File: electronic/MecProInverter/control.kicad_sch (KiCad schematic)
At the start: 30 parts, among them J5 Conn_01x08, SW1 PTS645SM95SMTR92LFS, SW2 PTS645SM95SMTR92LFS, SW3 PTS645SM95SMTR92LFS, U1 ESP32-S3-MINI-1-N8, U2 ADUM3160, U3 TYPE-C_16PIN_2MD(073), U6 SKRKAEE020, U7 SKRKAEE020

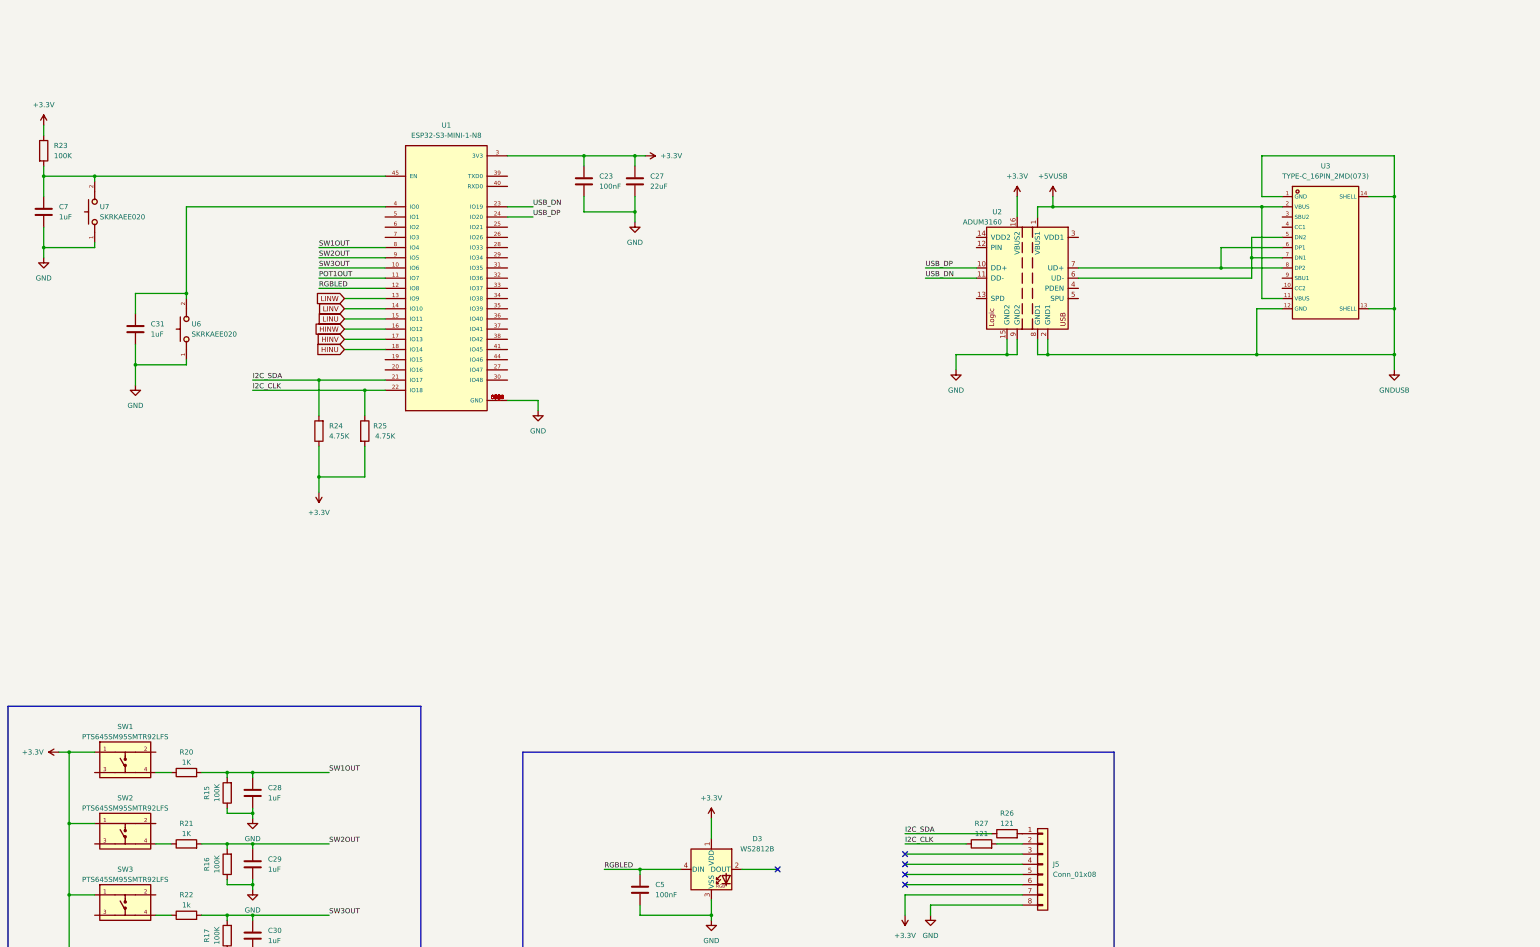
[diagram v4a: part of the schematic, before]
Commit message: electronic
-Control: Added Temp, Fan,
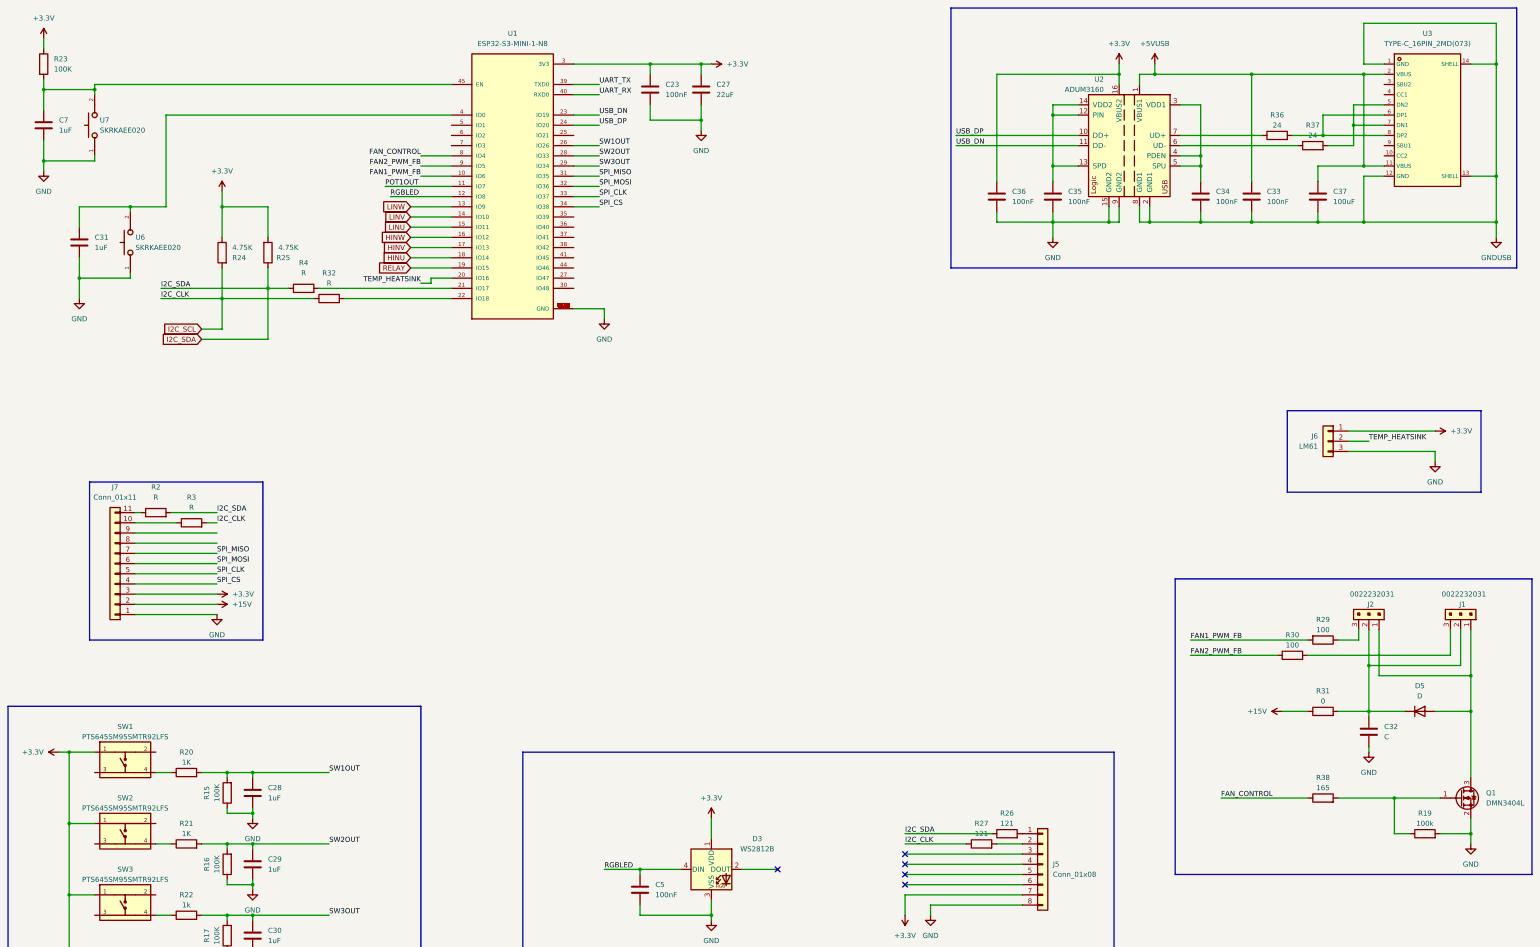
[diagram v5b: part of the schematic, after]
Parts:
- added C32: C, symbol Device:C
- added C33, C34, C35, C36: 100nF, symbol Device:C
- added C37: 100uF, symbol Device:C
- added D5: D, symbol Device:D
- added J1, J2: 0022232031, digikey-footprints:PinHeader_1x3_P2.54mm_Drill1.02mm, symbol dk_Rectangular-Connectors-Headers-Male-Pins:0022232031
- added J6: LM61, symbol Connector_Generic:Conn_01x03
- added J7: Conn_01x11, symbol Connector_Generic:Conn_01x11
- added Q1: DMN3404L, Package_TO_SOT_SMD:SOT-23, symbol Transistor_FET:DMN3404L
- added R19: 100k, symbol Device:R
- added R2, R3, R32, R4: R, symbol Device:R
- added R29, R30: 100, symbol Device:R
- added R31: 0, symbol Device:R
- added R36, R37: 24, symbol Device:R
- added R38: 165, symbol Device:R
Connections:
- net +3.3V: now also C36.1, J6.1 (Pin_1), J7.3 (Pin_3)
- net +5V: now also C33.1, C37.1
- net GND: now also C32.2, C33.2, C34.2, C35.2, C36.2, C37.2, J6.3 (Pin_3), J7.1 (Pin_1), Q1.2 (S), R19.2
- net I2C_SDA: now also R25.1, R2.2, R4.1; no longer R24.2, U1.21 (IO17)
- net SW1OUT: now also U1.26 (IO26); no longer U1.8 (IO4)
- net SW2OUT: now also U1.28 (IO33); no longer U1.9 (IO5)
- net SW3OUT: now also U1.29 (IO34); no longer U1.10 (IO6)
- net at U2.12 (PIN): now also U2.13 (SPD), U2.14 (VDD2), C35.1
- net at U2.3 (VDD1): now also U2.4 (PDEN), U2.5 (SPU), C34.1
- net at U3.5 (DN2), U3.7 (DN1): now also R37.2; no longer U2.6 (UD-)
- net at U3.6 (DP1), U3.8 (DP2): now also R36.2; no longer U2.7 (UD+)
- net RELAY: now reaches U1.19 (IO15)
- net TEMP_HEATSINK: now reaches U1.20 (IO16)
- net TEMP_HEATSINK: now also J6.2 (Pin_2)
- net SPI_MISO: now reaches U1.31 (IO35)
- net SPI_MISO: now also J7.7 (Pin_7)
- net SPI_MOSI: now reaches U1.32 (IO36)
- net SPI_MOSI: now also J7.6 (Pin_6)
- net SPI_CLK: now reaches U1.33 (IO37)
- net SPI_CLK: now also J7.5 (Pin_5)
- net SPI_CS: now reaches U1.34 (IO38)
- net SPI_CS: now also J7.4 (Pin_4)
- net UART_TX: now reaches U1.39 (TXD0)
- net UART_RX: now reaches U1.40 (RXD0)
- removed net I2C_CLK: R25.1, R27.1, U1.22 (IO18)
- new net: J7.10 (Pin_10), R3.1
- new net: J2.3, R29.1
- new net: Q1.1 (G), R19.1, R38.2
- new net: R37.1, U2.6 (UD-)
- new net: R36.1, U2.7 (UD+)
- new net: D5.2 (A), J1.1, J2.1, Q1.3 (D)
- new net: C32.1, D5.1 (K), J1.2, J2.2, R31.2
- new net: J1.3, R30.2
- new net: R4.2, U1.21 (IO17)
- new net: R32.2, U1.22 (IO18)
- new net: J7.11 (Pin_11), R2.1
- new net +15V: J7.2 (Pin_2), R31.1
- new net FAN1_PWM_FB: R29.2, U1.10 (IO6)
- new net FAN2_PWM_FB: R30.1, U1.9 (IO5)
- new net FAN_CONTROL: R38.1, U1.8 (IO4)
- new net I2C_SCL: R24.2, R27.1, R3.2, R32.1
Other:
- moved on the sheet: C23, C27, C31, C7, R23, R24, R25, U1, U2, U3, U6, U7

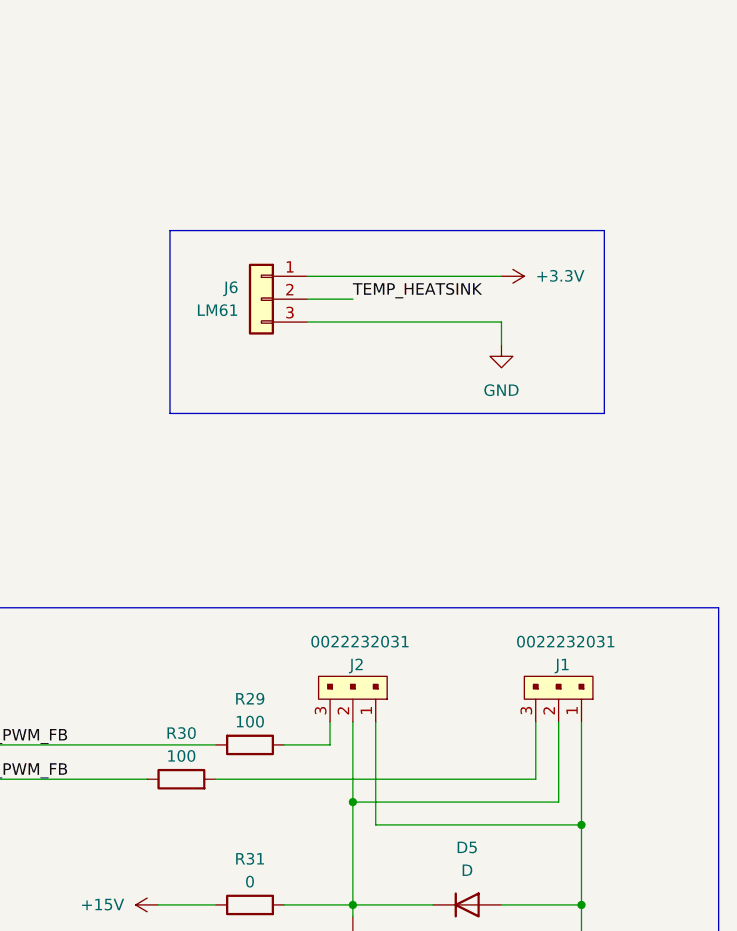
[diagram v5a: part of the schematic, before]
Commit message: electronic
Added: current sensor
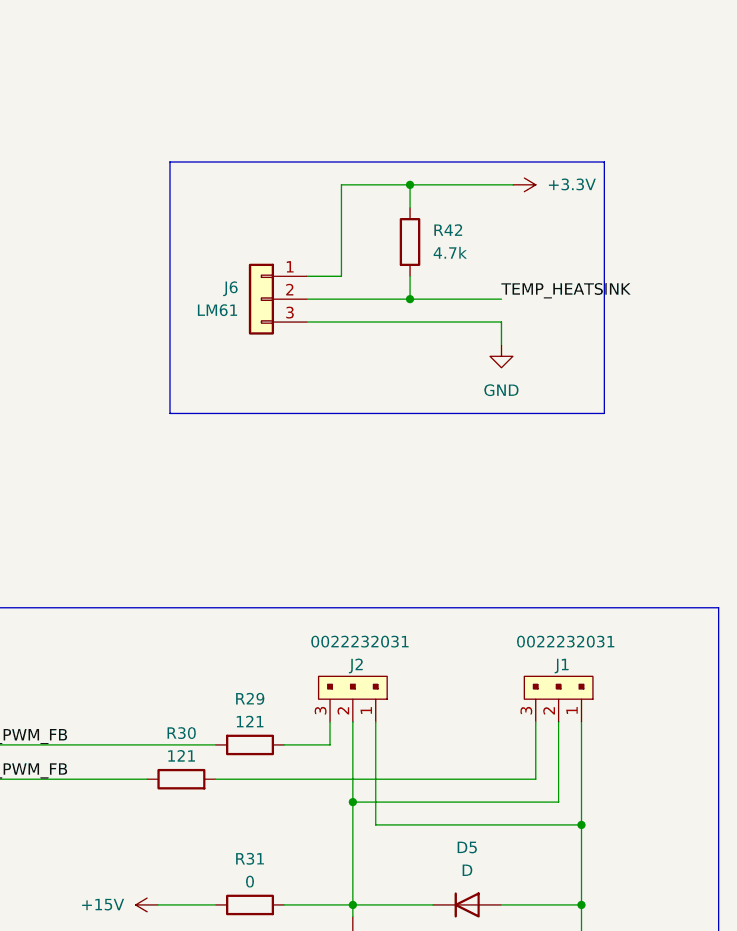
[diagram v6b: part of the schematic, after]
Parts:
- added R42: 4.7k, symbol Device:R
- J5: footprint (none) -> Connector_PinSocket_2.54mm:PinSocket_1x08_P2.54mm_Vertical
- J6: footprint (none) -> Connector_PinHeader_2.54mm:PinHeader_1x03_P2.54mm_Vertical
- J7: footprint (none) -> Connector_PinHeader_2.54mm:PinHeader_1x11_P2.54mm_Vertical
- R29, R30: value 100 -> 121
- U1: footprint ESP32-S3-MINI-1-N8:XCVR_ESP32-S3-MINI-1-N8 -> footprint:BULETM-SMD_ESP32-S3-MINI-1-N8
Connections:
- net +3.3V: now also R42.1
- net TEMP_HEATSINK: now also R42.2
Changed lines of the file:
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@@
   (junction (at 26.67 58.42) (diameter 0) (color 0 0 0 0)
   )
+  (junction (at 363.22 128.27) (diameter 0) (color 0 0 0 0)
+  )
   (junction (at 72.39 246.38) (diameter 0) (color 0 0 0 0)
   )
@@
   (junction (at 356.87 184.15) (diameter 0) (color 0 0 0 0)
   )
+  (junction (at 363.22 115.57) (diameter 0) (color 0 0 0 0)
+  )
   (junction (at 71.12 92.71) (diameter 0) (color 0 0 0 0)
   )
@@
     (stroke (width 0) (type default))
   )
-  (wire (pts (xy 373.38 125.73) (xy 351.79 125.73))
+  (wire (pts (xy 374.65 115.57) (xy 363.22 115.57))
     (stroke (width 0) (type default))
   )
@@
     (stroke (width 0) (type default))
   )
+  (wire (pts (xy 355.6 125.73) (xy 351.79 125.73))
+    (stroke (width 0) (type default))
+  )
+  (wire (pts (xy 363.22 125.73) (xy 363.22 128.27))
+    (stroke (width 0) (type default))
+  )
   (wire (pts (xy 66.04 210.82) (xy 72.39 210.82))
     (stroke (width 0) (type default))
@@
     (stroke (width 0) (type default))
   )
+  (wire (pts (xy 363.22 115.57) (xy 363.22 118.11))
+    (stroke (width 0) (type default))
+  )
   (wire (pts (xy 327.66 36.83) (xy 355.6 36.83))
     (stroke (width 0) (type default))
@@
     (stroke (width 0) (type default))
   )
+  (wire (pts (xy 355.6 115.57) (xy 355.6 125.73))
+    (stroke (width 0) (type default))
+  )
   (wire (pts (xy 363.22 226.06) (xy 363.22 217.17))
     (stroke (width 0) (type default))
@@
     (stroke (width 0) (type default))
   )
+  (wire (pts (xy 363.22 115.57) (xy 355.6 115.57))
+    (stroke (width 0) (type default))
+  )
   (wire (pts (xy 66.04 228.6) (xy 72.39 228.6))
     (stroke (width 0) (type default))
@@
     (stroke (width 0) (type default))
   )
-  (wire (pts (xy 356.87 128.27) (xy 351.79 128.27))
+  (wire (pts (xy 373.38 128.27) (xy 363.22 128.27))
     (stroke (width 0) (type default))
   )
@@
     (stroke (width 0) (type default))
   )
+  (wire (pts (xy 363.22 128.27) (xy 351.79 128.27))
+    (stroke (width 0) (type default))
+  )
   (wire (pts (xy 382.27 186.69) (xy 382.27 195.58))
     (stroke (width 0) (type default))
@@
     (fill (type none))
   )
-  (rectangle (start 336.55 120.65) (end 384.81 140.97)
+  (rectangle (start 336.55 113.03) (end 384.81 140.97)
     (stroke (width 0) (type default))
     (fill (type none))
@@
     (effects (font (size 1.27 1.27)) (justify left bottom))
   )
-  (label "TEMP_HEATSINK" (at 356.87 128.27 0) (fields_autoplaced)
+  (label "TEMP_HEATSINK" (at 373.38 128.27 0) (fields_autoplaced)
     (effects (font (size 1.27 1.27)) (justify left bottom))
   )
@@
       (effects (font (size 1.27 1.27)))
     )
-    (property "Value" "100" (at 345.44 175.26 90)
+    (property "Value" "121" (at 345.44 175.26 90)
       (effects (font (size 1.27 1.27)))
     )
@@
       (effects (font (size 1.27 1.27)) (justify left))
     )
-    (property "Footprint" "" (at 346.71 128.27 0)
+    (property "Footprint" "Connector_PinHeader_2.54mm:PinHeader_1x03_P2.54mm_Vertical" (at 346.71 128.27 0)
       (effects (font (size 1.27 1.27)) hide)
     )
@@
     )
   )
-  (symbol (lib_id "power:+3.3V") (at 373.38 125.73 270) (mirror x) (unit 1)
+  (symbol (lib_id "power:+3.3V") (at 374.65 115.57 270) (mirror x) (unit 1)
     (in_bom yes) (on_board yes) (dnp no) (fields_autoplaced)
-    (property "Reference" "#PWR037" (at 369.57 125.73 0)
+    (property "Reference" "#PWR037" (at 370.84 115.57 0)
       (effects (font (size 1.27 1.27)) hide)
     )
-    (property "Value" "+3.3V" (at 377.19 125.73 90)
+    (property "Value" "+3.3V" (at 378.46 115.57 90)
       (effects (font (size 1.27 1.27)) (justify left))
     )
-    (property "Footprint" "" (at 373.38 125.73 0)
+    (property "Footprint" "" (at 374.65 115.57 0)
       (effects (font (size 1.27 1.27)) hide)
     )
-    (property "Datasheet" "" (at 373.38 125.73 0)
+    (property "Datasheet" "" (at 374.65 115.57 0)
       (effects (font (size 1.27 1.27)) hide)
     )
@@
       (effects (font (size 1.27 1.27)))
     )
-    (property "Footprint" "ESP32-S3-MINI-1-N8:XCVR_ESP32-S3-MINI-1-N8" (at 143.51 64.77 0)
+    (property "Footprint" "footprint:BULETM-SMD_ESP32-S3-MINI-1-N8" (at 143.51 64.77 0)
       (effects (font (size 1.27 1.27)) (justify bottom) hide)
     )
@@
       (effects (font (size 1.27 1.27)) (justify left))
     )
-    (property "Footprint" "" (at 275.59 233.68 0)
+    (property "Footprint" "Connector_PinSocket_2.54mm:PinSocket_1x08_P2.54mm_Vertical" (at 275.59 233.68 0)
       (effects (font (size 1.27 1.27)) hide)
     )
@@
       (effects (font (size 1.27 1.27)))
     )
-    (property "Value" "100" (at 337.82 179.07 90)
+    (property "Value" "121" (at 337.82 179.07 90)
       (effects (font (size 1.27 1.27)))
     )
@@
       (effects (font (size 1.27 1.27)))
     )
-    (property "Footprint" "" (at 44.45 158.75 0)
+    (property "Footprint" "Connector_PinHeader_2.54mm:PinHeader_1x11_P2.54mm_Vertical" (at 44.45 158.75 0)
       (effects (font (size 1.27 1.27)) hide)
     )
@@
     )
   )
+  (symbol (lib_id "Device:R") (at 363.22 121.92 0) (unit 1)
+    (in_bom yes) (on_board yes) (dnp no) (fields_autoplaced)
+    (property "Reference" "R42" (at 365.76 120.65 0)
+      (effects (font (size 1.27 1.27)) (justify left))
+    )
+    (property "Value" "4.7k" (at 365.76 123.19 0)
+      (effects (font (size 1.27 1.27)) (justify left))
+    )
+    (property "Footprint" "" (at 361.442 121.92 90)
+      (effects (font (size 1.27 1.27)) hide)
+    )
+    (property "Datasheet" "~" (at 363.22 121.92 0)
+      (effects (font (size 1.27 1.27)) hide)
+    )
+    (pin "1")
+    (pin "2")
+    (instances
+      (project "MecProInverter"
+        (path "/c9071429-8b0d-45bf-aa6d-71cc2b7f068c/87c5d68c-a194-45d1-987f-2b491b6ac1ab"
+          (reference "R42") (unit 1)
+        )
+      )
+    )
+  )
   (symbol (lib_id "my_power:+5VUSB") (at 303.53 34.29 0) (unit 1)
     (in_bom yes) (on_board yes) (dnp no) (fields_autoplaced)
@@
   (symbol (lib_id "power:GND") (at 78.74 240.03 0) (unit 1)
     (in_bom yes) (on_board yes) (dnp no) (fields_autoplaced)
-    (property "Reference" "#PWR?" (at 78.74 246.38 0)
+    (property "Reference" "#PWR0101" (at 78.74 246.38 0)
       (effects (font (size 1.27 1.27)) hide)
     )
@@
       (project "MecProInverter"
         (path "/c9071429-8b0d-45bf-aa6d-71cc2b7f068c/87c5d68c-a194-45d1-987f-2b491b6ac1ab"
-          (reference "#PWR?") (unit 1)
+          (reference "#PWR0101") (unit 1)
         )
       )
